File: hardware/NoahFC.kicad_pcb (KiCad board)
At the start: 2 copper layers, 36 x 40 mm, 44 parts, among them J1 ALE, J11 SCK, J12 MISO, J17 VTX, J18 RESET, J2 ELE, J3 CAM, J4 FTDI, J5 VCC, J6 THR, J7 PPM, J8 GPS, U1 ATmega328, U2 MPU-6050, U4 AMS1117-3.3, U5 MAX7456EUI+, U6 HMC5883L, Y1 16Mhz, Y2 27Mhz

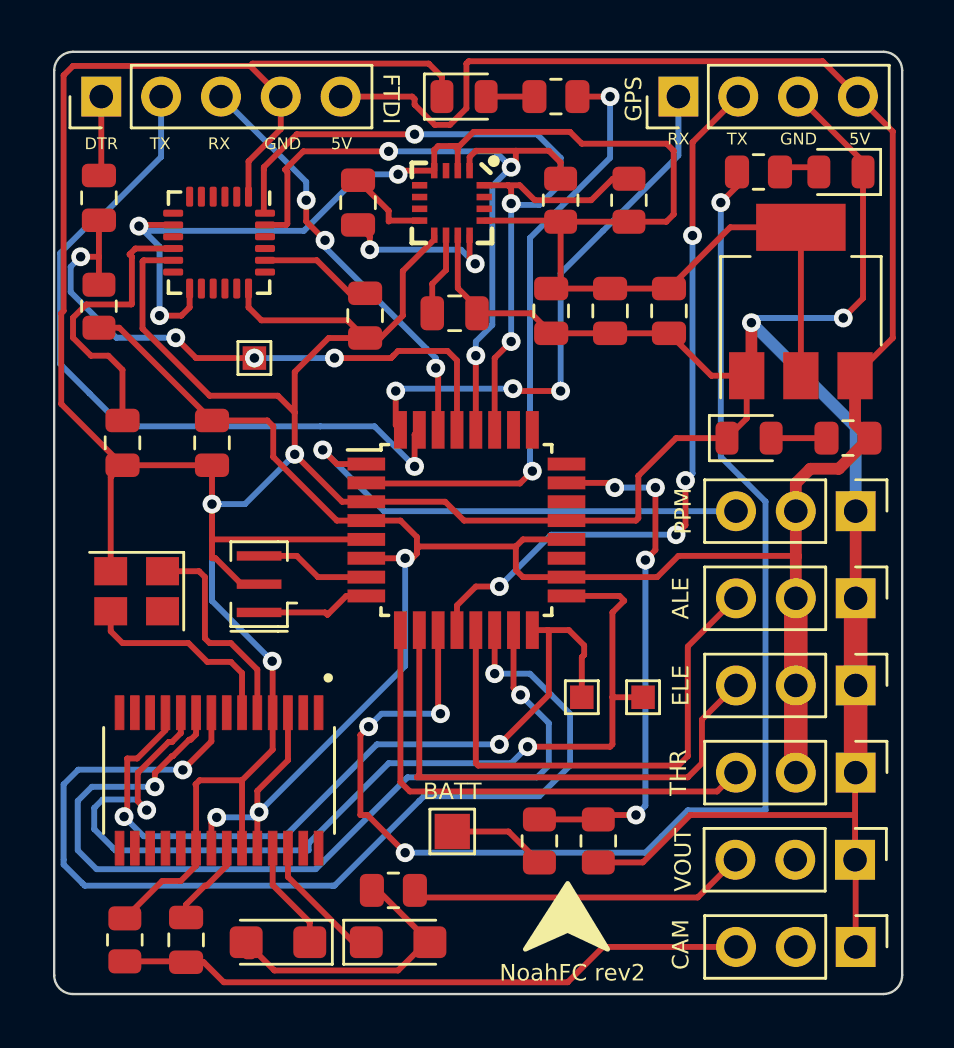
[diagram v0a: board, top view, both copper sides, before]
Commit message: rename folder
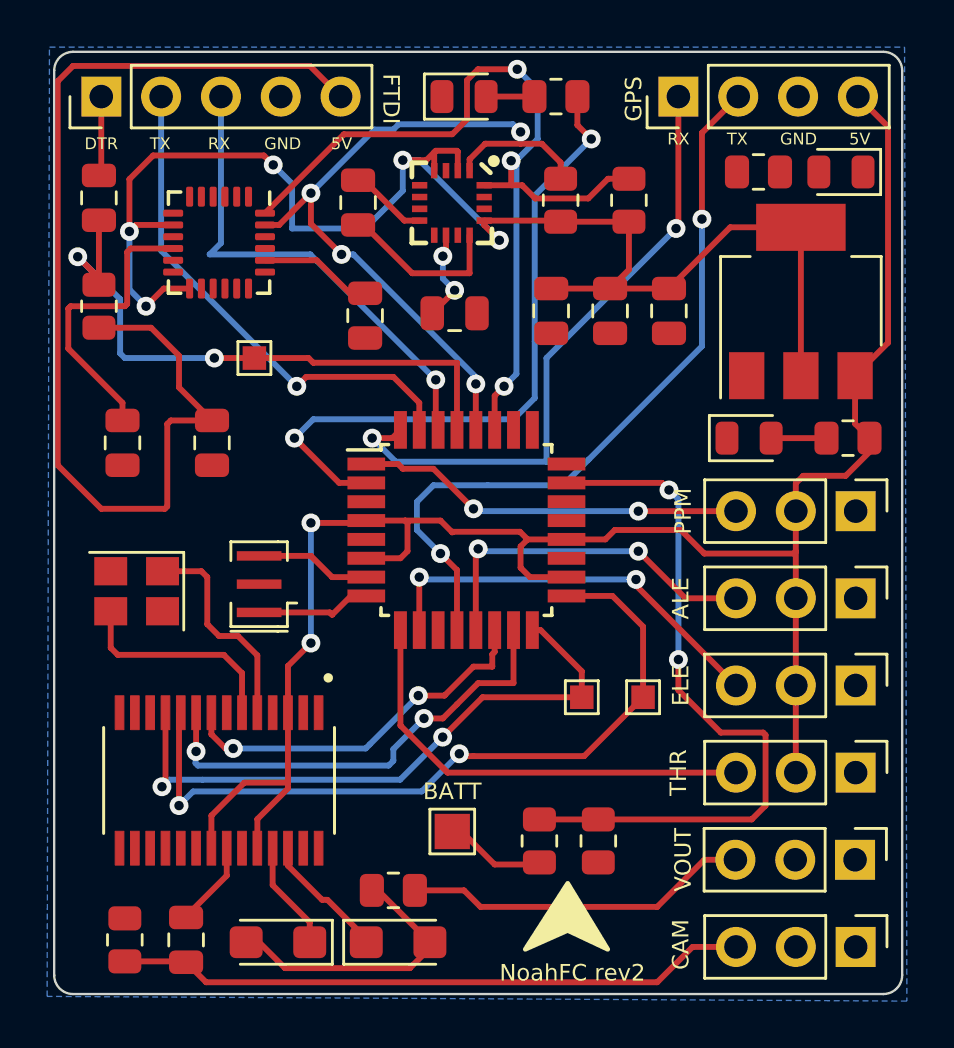
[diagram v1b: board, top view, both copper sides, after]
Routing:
- net GND: track 222.7 -> 0.00 mm, vias 5 -> 0
- net LED_GPS: track 58.4 -> 0.00 mm, vias 4 -> 0
- net SS: track 43.6 -> 16.1 mm
- net MOSI: track 38.1 -> 19.7 mm
- net SCK: track 43.1 -> 32.5 mm
- net TX: track 31.7 -> 21.7 mm
- net VOLTAGE_READ: track 22.3 -> 30.5 mm, vias 4 -> 2
- net MISO: track 33.7 -> 26.5 mm
- net ALERON: track 22.4 -> 15.3 mm, vias 0 -> 2
- net 5V: track 121.4 -> 127.9 mm, vias 3 -> 2
- net ELEVATOR: track 22.5 -> 17.7 mm, vias 0 -> 2
- net PPM: track 20.7 -> 16.5 mm, vias 1 -> 2
- net GPS_RX: track 23.4 -> 27.0 mm, vias 3 -> 2
- net RX: track 18.0 -> 20.9 mm, vias 3 -> 1
- net LED_MODE: track 26.0 -> 28.8 mm
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- added copper zone on B.Cu, net GND

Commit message: route rev2
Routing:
- net GND: track 0.00 -> 98.7 mm, vias 0 -> 18
- net LED_GPS: track 0.00 -> 33.0 mm, vias 0 -> 2
- net 5V: track 127.9 -> 134.9 mm
- net Net-(D1-Pad2): track 0.00 -> 1.65 mm
- net Net-(C21-Pad1): track 7.20 -> 8.81 mm
- net 3.3V: track 64.2 -> 63.4 mm
- net SCL: track 32.1 -> 32.9 mm
- net SDA: track 38.7 -> 39.4 mm

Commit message: small tidy in firmware
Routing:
- net GND: track 98.7 -> 101.6 mm
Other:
- board text added: "BAT"
- board text added: "VTX"
- board text removed: "BATT"
- board text removed: "VOUT"

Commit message: rev4 project
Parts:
- removed C20: 4.7uF, Capacitor_SMD:C_0805_2012Metric
- removed C21: 220nF, Capacitor_SMD:C_0805_2012Metric
- removed D3: PWR, LED_SMD:LED_0805_2012Metric
- removed J1: ALE, Connector_PinHeader_2.54mm:PinHeader_1x03_P2.54mm_Vertical
- removed J11: SCK, TestPoint:TestPoint_Pad_1.0x1.0mm
- removed J12: MISO, TestPoint:TestPoint_Pad_1.0x1.0mm
- removed J17: VTX, Connector_PinHeader_2.54mm:PinHeader_1x03_P2.54mm_Vertical
- removed J18: RESET, TestPoint:TestPoint_Pad_1.0x1.0mm
- removed J2: ELE, Connector_PinHeader_2.54mm:PinHeader_1x03_P2.54mm_Vertical
- removed J3: CAM, Connector_PinHeader_2.54mm:PinHeader_1x03_P2.54mm_Vertical
- removed J4: FTDI, Connector_PinHeader_2.54mm:PinHeader_1x05_P2.54mm_Vertical
- removed J6: THR, Connector_PinHeader_2.54mm:PinHeader_1x03_P2.54mm_Vertical
- removed J7: PPM, Connector_PinHeader_2.54mm:PinHeader_1x03_P2.54mm_Vertical
- removed J8: GPS, Connector_PinHeader_2.54mm:PinHeader_1x04_P2.54mm_Vertical
- removed R4: 330, Resistor_SMD:R_0805_2012Metric
- removed U6: HMC5883L, HMC5883L:LPCC-16
- removed Y2: 27Mhz, Crystal:Crystal_SMD_3225-4Pin_3.2x2.5mm
- added ALE: ALE, Connector_PinHeader_2.54mm:PinHeader_1x03_P2.54mm_Vertical, F.Cu at (68.6, 75.5)
- added C1: 100nF, Capacitor_SMD:C_0805_2012Metric, F.Cu at (70.4, 113.7)
- added C2: 100nF, Capacitor_SMD:C_0805_2012Metric, F.Cu at (76.3, 102.5)
- added C4: 100nF, Capacitor_SMD:C_0805_2012Metric, F.Cu at (74.1, 113.7)
- added ELE: ELE, Connector_PinHeader_2.54mm:PinHeader_1x03_P2.54mm_Vertical, F.Cu at (72.2, 75.5)
- added FTDI: FTDI, Connector_JST:JST_SH_BM05B-SRSS-TB_1x05-1MP_P1.00mm_Vertical, F.Cu at (65.2, 88.2)
- added GPS: GPS, Connector_JST:JST_SH_BM04B-SRSS-TB_1x04-1MP_P1.00mm_Vertical, F.Cu at (65.2, 96.6)
- added OSD: OSD, Connector_JST:JST_SH_BM05B-SRSS-TB_1x05-1MP_P1.00mm_Vertical, F.Cu at (91.2, 106.0)
- added PPM: PPM, Connector_PinHeader_2.54mm:PinHeader_1x03_P2.54mm_Vertical, F.Cu at (79.4, 75.5)
- added THR: THR, Connector_PinHeader_2.54mm:PinHeader_1x03_P2.54mm_Vertical, F.Cu at (75.8, 75.5)
- added Y3: 27Mhz, Crystal:Crystal_SMD_3225-4Pin_3.2x2.5mm, F.Cu at (71.3, 101.2)
- C11: value 22uF -> 10uF
- R7, R8: value 10K -> 4.7K
- moved D1 89.9 mm to (64.8, 104.3)
- moved R2 85.9 mm to (64.8, 102.0), turned to 180 degrees
- moved R3 74.7 mm to (64.7, 81.4)
- moved D2 70.6 mm to (64.7, 79.1), turned to 180 degrees
- moved U4 59.7 mm to (90.2, 91.8)
- moved R6 59.3 mm to (85.1, 88.5), turned to 90 degrees
- moved U1 57.9 mm to (77.7, 90.7)
- moved C6 56.9 mm to (88.0, 75.6), turned to 180 degrees
- moved Y1 56.5 mm to (70.4, 91.5)
- moved C7 56.4 mm to (82.9, 79.8), turned to 90 degrees
- moved R5 55.7 mm to (85.1, 92.2)
- moved C11 54.1 mm to (88.8, 97.9), turned to 0 degrees
- moved U5 52.4 mm to (72.6, 108.2)
- moved R8 51.4 mm to (91.0, 84.9), turned to 180 degrees
- moved C19 51.2 mm to (81.5, 107.5)
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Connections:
- net Net-(C17-Pad1) renamed VIN
- C18 pad 1: Net-(C18-Pad1) -> VOUT
- C19 pad 1: Net-(C19-Pad1) -> SAG
- C6 pad 1: GND -> 3.3V
- C6 pad 2: 3.3V -> GND
- C7 pad 1: 3.3V -> GND
- C7 pad 2: GND -> 3.3V
- R7 pad 2: SCL -> SDA
- R8 pad 2: SDA -> SCL
- U5 pad 19: unconnected-(U5-Pad19) -> 5V
- U5 pad 25: Net-(C18-Pad1) -> SAG
- U5 pad 26: Net-(C19-Pad1) -> VOUT
- U5 pad 5: XTAL2_OSD -> XTAL1_OSD
- U5 pad 6: XTAL1_OSD -> XTAL2_OSD
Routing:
- net GND: track 101.6 -> 53.6 mm, vias 18 -> 21
- net 5V: track 134.9 -> 168.4 mm, vias 2 -> 6
- net VOLTAGE_READ: track 30.5 -> 5.34 mm, vias 2 -> 0
- net 3.3V: track 63.4 -> 41.0 mm, vias 5 -> 0
- net GPS_TX: track 32.2 -> 14.1 mm
- net LED_GPS: track 33.0 -> 15.0 mm, vias 2 -> 0
- net SDA: track 39.4 -> 24.5 mm, vias 3 -> 0
- net ALERON: track 15.3 -> 28.3 mm
- net SCL: track 32.9 -> 20.4 mm, vias 4 -> 0
- net LED_MODE: track 28.8 -> 17.2 mm, vias 2 -> 4
- net Net-(J13-Pin_3): track 14.7 -> 3.49 mm
- net Net-(J13-Pin_1): track 26.9 -> 18.0 mm
- net VIN: track 3.66 -> 12.6 mm, vias 0 -> 2
- net Net-(C21-Pad1): track 8.81 -> 0.00 mm
- net Net-(U2-REGOUT): track 12.5 -> 3.72 mm
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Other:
- board size 36 x 40 mm -> 32 x 42 mm
- board text added: "NoahFC rev4"
- board text removed: "5V"
- board text removed: "ALE"
- board text removed: "BAT"
- board text removed: "CAM"
- board text removed: "DTR"
- board text removed: "ELE"
- board text removed: "FTDI"
- board text removed: "GND"
- board text removed: "GPS"
- board text removed: "NoahFC rev2"
- board text removed: "PPM"
- board text removed: "RX"
- board text removed: "THR"
- board text removed: "TX"
- board text removed: "VTX"

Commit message: add bottom labels
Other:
- board text added: "5V GND VTX GND CAM"
- board text added: "DTR TX RX GND 5V"
- board text added: "RX TX GND 5V"
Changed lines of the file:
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@@
   (gr_arc locked (start 64.2 115.2) (mid 62.785786 114.614214) (end 62.2 113.2)
     (stroke (width 0.2) (type solid)) (layer "Edge.Cuts"))
+  (gr_text "RX TX GND 5V" (at 63.9 100.1 270) (layer "B.SilkS")
+    (effects (font (size 0.6 0.6) (thickness 0.15)) (justify left bottom mirror))
+  )
+  (gr_text "DTR TX RX GND 5V" (at 63.8 92.5 270) (layer "B.SilkS")
+    (effects (font (size 0.6 0.6) (thickness 0.15)) (justify left bottom mirror))
+  )
+  (gr_text "5V GND VTX GND CAM" (at 92.2 110.9 270) (layer "B.SilkS")
+    (effects (font (size 0.6 0.6) (thickness 0.15)) (justify left bottom mirror))
+  )
   (gr_text "http://github.com/zosko/NoahFC\n\nby Bosko " (at 78 101.2) (layer "B.SilkS")
     (effects (font (size 1 1) (thickness 0.15)) (justify mirror))

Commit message: update project rev5
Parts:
- removed J5: VCC, TestPoint:TestPoint_Pad_1.5x1.5mm
- removed R5: 100K, Resistor_SMD:R_0805_2012Metric
- removed R6: 10K, Resistor_SMD:R_0805_2012Metric
- removed U4: AMS1117-3.3, Package_TO_SOT_SMD:SOT-223-3_TabPin2
- added U3: XC6206PxxxMR, Package_TO_SOT_SMD:SOT-23-3, F.Cu at (87.0, 89.0)
- C10, C11: value 10uF -> 1uF
- moved C8 10.3 mm to (89.2, 84.7), turned to 0 degrees
- moved R8 9.58 mm to (88.0, 75.8), turned to -90 degrees
- moved C6 9.49 mm to (85.3, 84.7)
- moved C11 9.00 mm to (90.7, 89.1), turned to 90 degrees
- moved C7 8.55 mm to (91.3, 81.4), turned to 180 degrees
- moved C10 8.45 mm to (87.1, 92.2), turned to 180 degrees
- moved C9 7.81 mm to (91.3, 78.9), turned to 0 degrees
- moved R7 7.49 mm to (85.8, 75.8)
- moved Y1 4.62 mm to (70.0, 96.1), turned to 180 degrees
- moved D1 3.90 mm to (64.8, 108.2)
- moved R2 3.90 mm to (64.8, 105.9)
- moved C3 3.83 mm to (70.7, 91.0)
- moved R1 3.14 mm to (70.7, 87.5), turned to -90 degrees
- moved J8 2.80 mm to (65.3, 99.4)
- moved J4 2.10 mm to (65.3, 90.3)
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- renumbered ALE to J1, OSD to J13, ELE to J2, FTDI to J4, THR to J6, PPM to J7, GPS to J8
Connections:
- U1 pad 23: VOLTAGE_READ -> unconnected-(U1-PC0-Pad23)
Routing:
- net GND: track 53.6 -> 67.8 mm, vias 21 -> 16
- net SDA: track 24.5 -> 16.8 mm
- net RESET: track 21.0 -> 28.0 mm
- net RX: track 14.8 -> 21.4 mm
- net 5V: track 168.4 -> 174.6 mm
- net VOLTAGE_READ: track 5.34 -> 0.00 mm
- net 3.3V: track 41.0 -> 36.5 mm, vias 0 -> 2
- net GPS_RX: track 23.8 -> 28.1 mm, vias 2 -> 0
- net Net-(J5-Pin_1): track 3.67 -> 0.00 mm
- net DTR: track 3.64 -> 7.21 mm, vias 0 -> 2
- net LED_GPS: track 15.0 -> 18.3 mm
- net SCL: track 20.4 -> 23.3 mm
- net TX: track 13.7 -> 16.6 mm
- net Net-(U2-CPOUT): track 2.71 -> 4.65 mm
- net LED_MODE: track 17.2 -> 18.4 mm
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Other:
- board text added: "NoahFC rev5"
- board text removed: "NoahFC rev4"

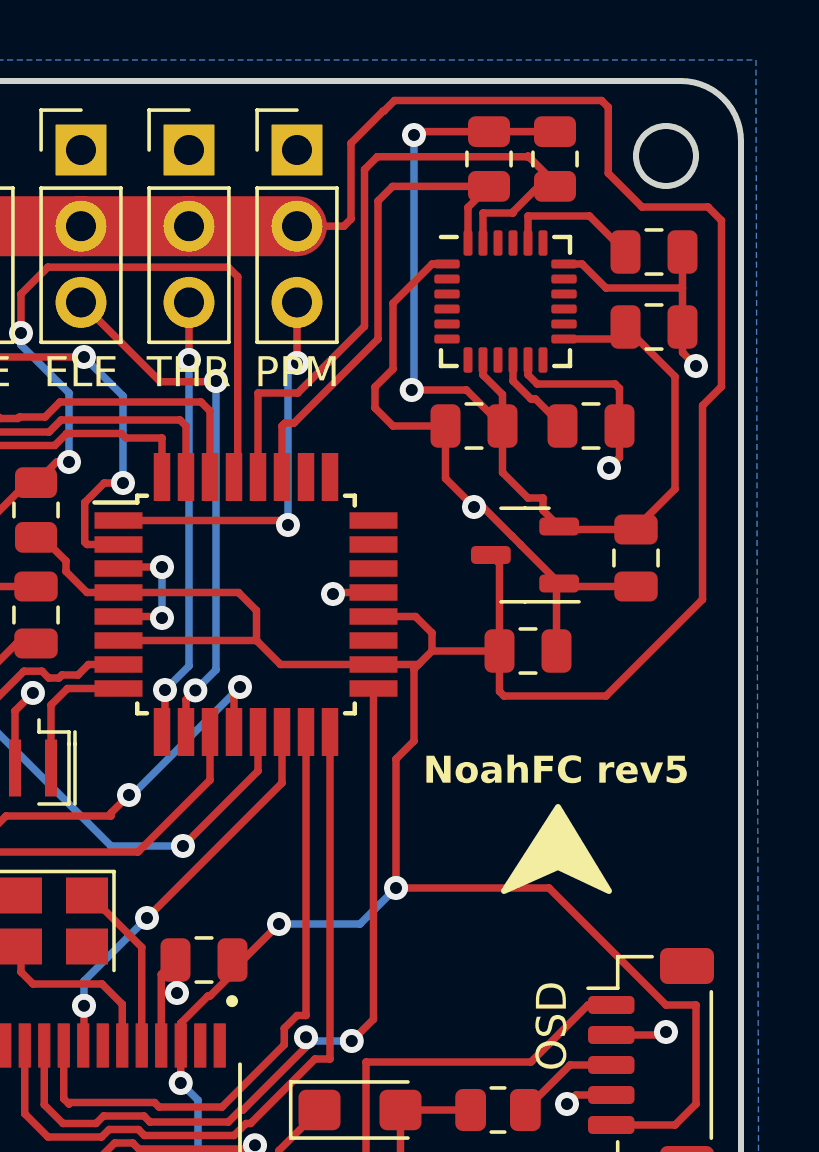
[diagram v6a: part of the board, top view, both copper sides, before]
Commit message: add sda scl pinout
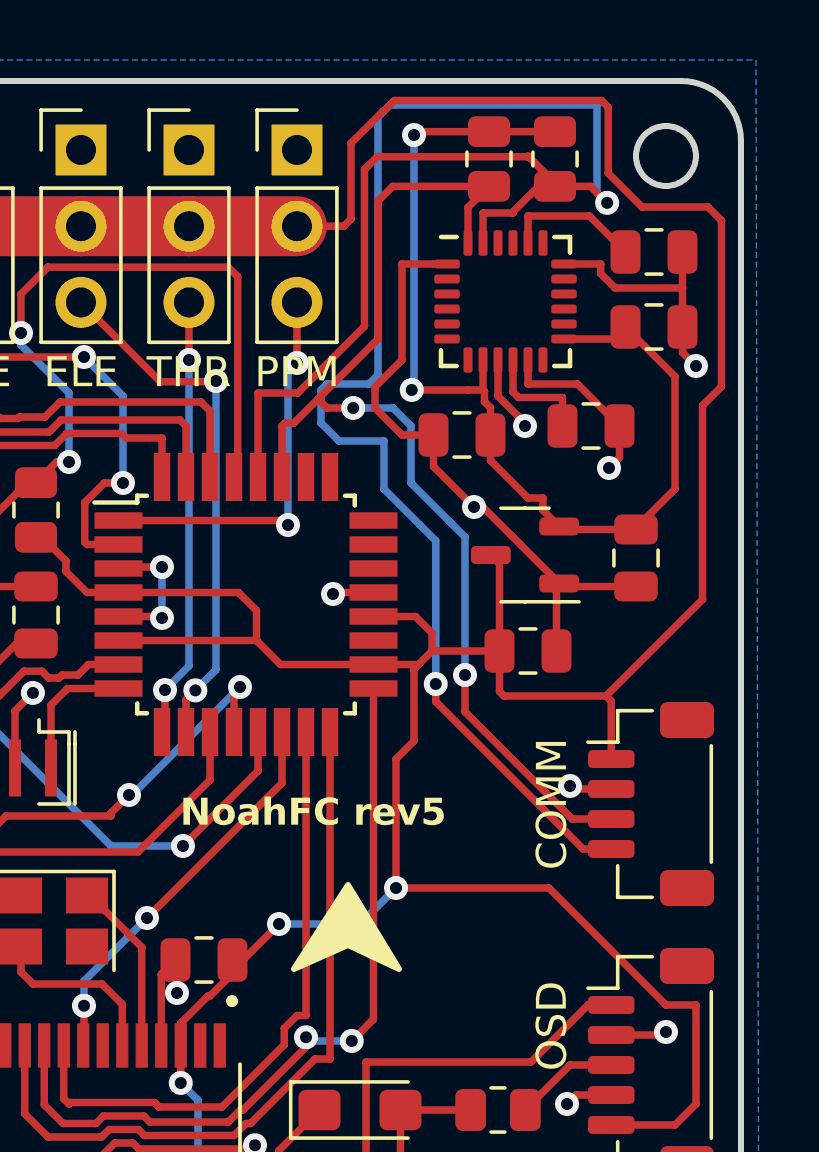
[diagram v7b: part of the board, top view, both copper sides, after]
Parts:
- added J3: COMM, Connector_JST:JST_SH_BM04B-SRSS-TB_1x04-1MP_P1.00mm_Vertical, F.Cu at (91.2, 97.3)
- moved C6 0.50 mm to (84.9, 85.0)
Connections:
- U2 pad 9: unconnected-(U2-AD0-Pad9) -> GND
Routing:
- net SCL: track 23.3 -> 67.6 mm, vias 0 -> 2
- net SDA: track 16.8 -> 36.9 mm, vias 0 -> 2
- net GND: track 67.8 -> 71.6 mm, vias 16 -> 18
- net 5V: track 174.6 -> 176.8 mm
- net 3.3V: track 36.5 -> 35.3 mm
- net Net-(U2-REGOUT): track 2.97 -> 3.74 mm

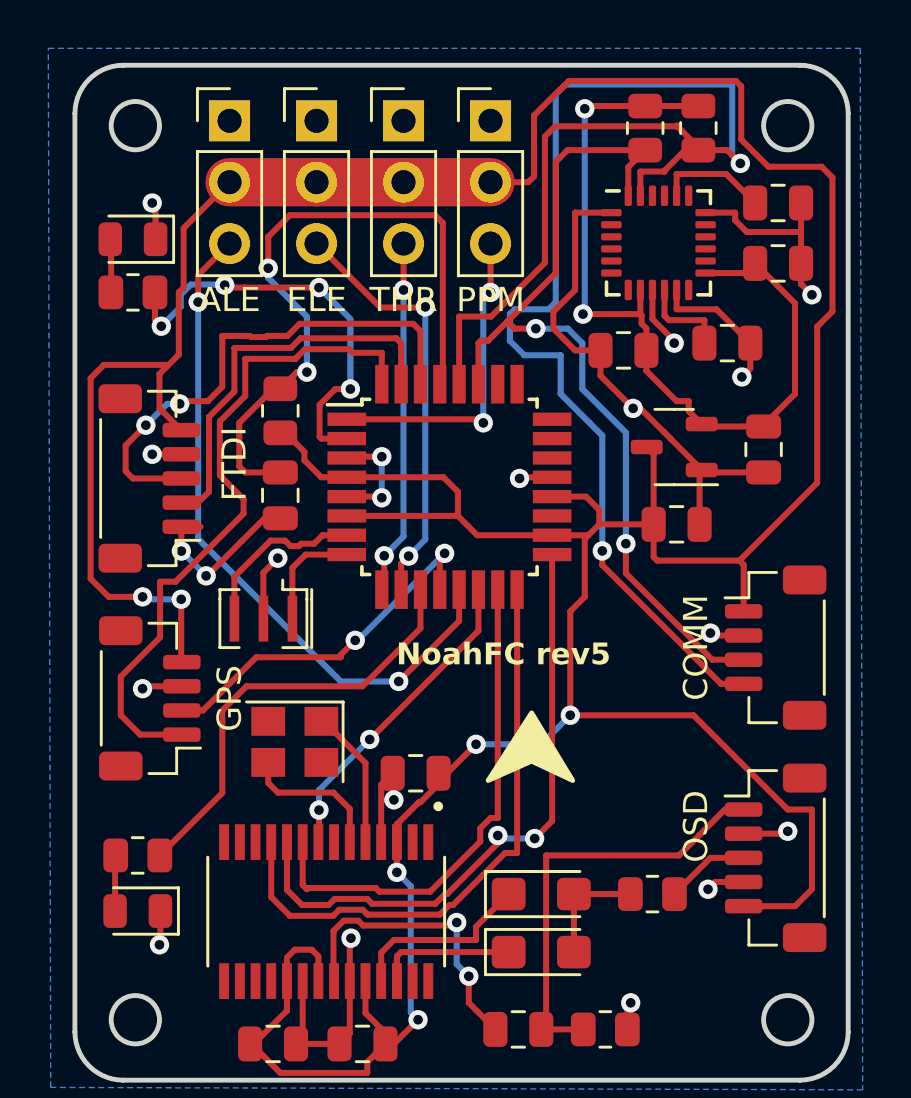
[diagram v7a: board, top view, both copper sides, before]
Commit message: add jumper, organize pcb
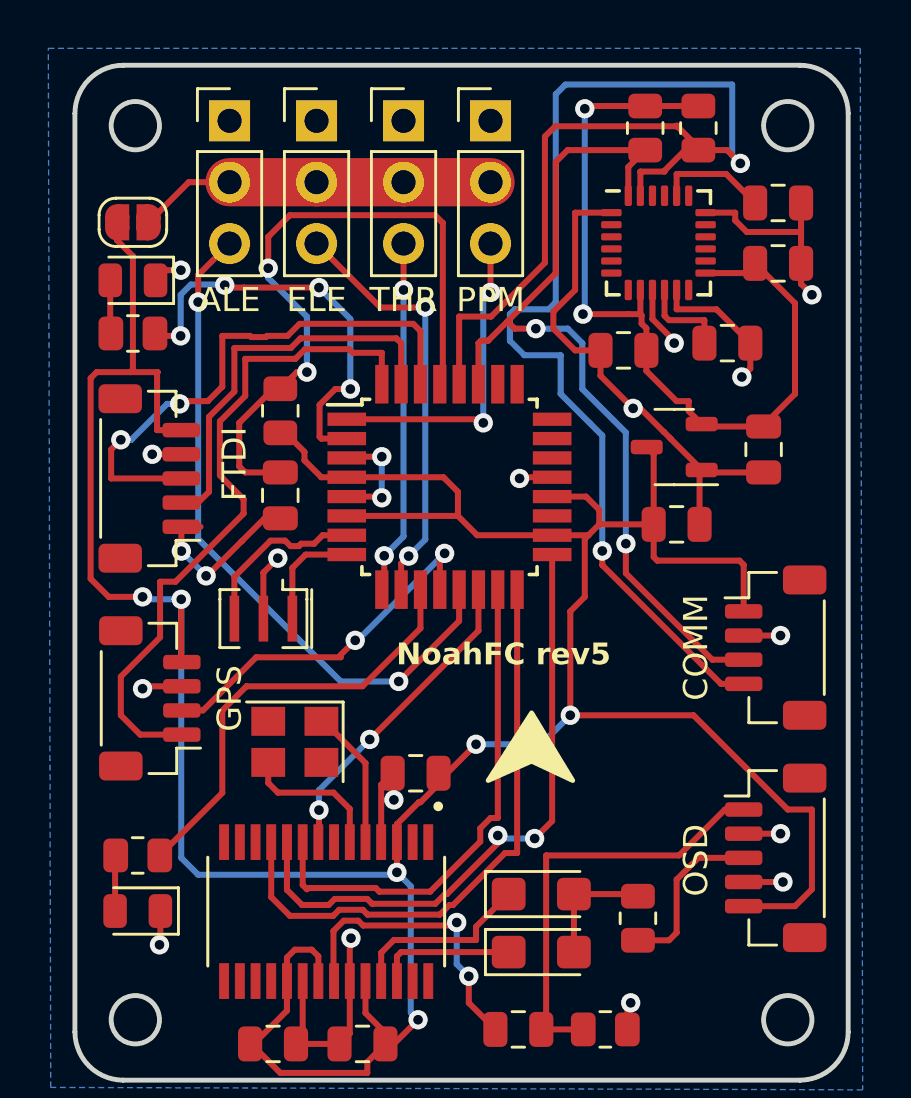
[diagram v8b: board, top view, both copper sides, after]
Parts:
- added JP1: power from servo, Jumper:SolderJumper-2_P1.3mm_Open_RoundedPad1.0x1.5mm, F.Cu at (64.6, 79.7)
- U3: value XC6206PxxxMR -> XC6206P332MR
- moved R3 1.70 mm to (64.6, 84.3)
- moved D2 1.70 mm to (64.6, 82.1)
- moved R10 1.17 mm to (85.5, 108.5), turned to -90 degrees
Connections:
- J1 pad 2: 5V -> 5V-BEC
- J2 pad 2: 5V -> 5V-BEC
- J6 pad 2: 5V -> 5V-BEC
- J7 pad 2: 5V -> 5V-BEC
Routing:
- net 5V: track 176.8 -> 145.8 mm
- net 5V-BEC: track 0.00 -> 14.8 mm
- net Net-(J13-Pin_3): track 3.49 -> 7.08 mm
- net RX: track 21.4 -> 22.6 mm
- net LED_MODE: track 18.4 -> 17.5 mm
- net GND: track 71.6 -> 71.0 mm
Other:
- board text added: "SCL SDA GND 5V"
